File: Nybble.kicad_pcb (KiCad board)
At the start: 2 copper layers, 250.4 x 79 mm, 106 parts, among them J1 USB_mini_micro_B, SW1 SW_PUSH, U1 ATMEGA32U4, X1 XTAL_GND

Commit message: Starting to add traces to keyboard
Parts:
- moved C1 8.55 mm to (100.2, 86.0), turned to 45 degrees
- moved C2 4.56 mm to (96.2, 90.0), turned to 225 degrees
- moved C6 3.70 mm to (85.9, 90.7), turned to 270 degrees
- moved X1 2.16 mm to (95.6, 86.0), turned to 225 degrees
- moved R2 2.03 mm to (83.8, 90.9), turned to 270 degrees
- moved C7 1.91 mm to (84.0, 69.7)
- moved C3 1.30 mm to (77.6, 75.3), turned to 225 degrees
- turned SW1 to 180 degrees
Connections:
- MX27 pad 2: Net-(MX27-Pad2) -> Net-(D27-Pad2)
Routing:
- net VCC: track 0.00 -> 208.5 mm, vias 0 -> 4
- net Net-(C2-Pad1): track 0.00 -> 12.2 mm
- net Net-(R2-Pad1): track 0.00 -> 11.3 mm, vias 0 -> 2
- net Net-(C1-Pad1): track 0.00 -> 11.2 mm
- net Net-(R1-Pad2): track 0.00 -> 4.34 mm
- net Net-(C8-Pad1): track 0.00 -> 3.70 mm

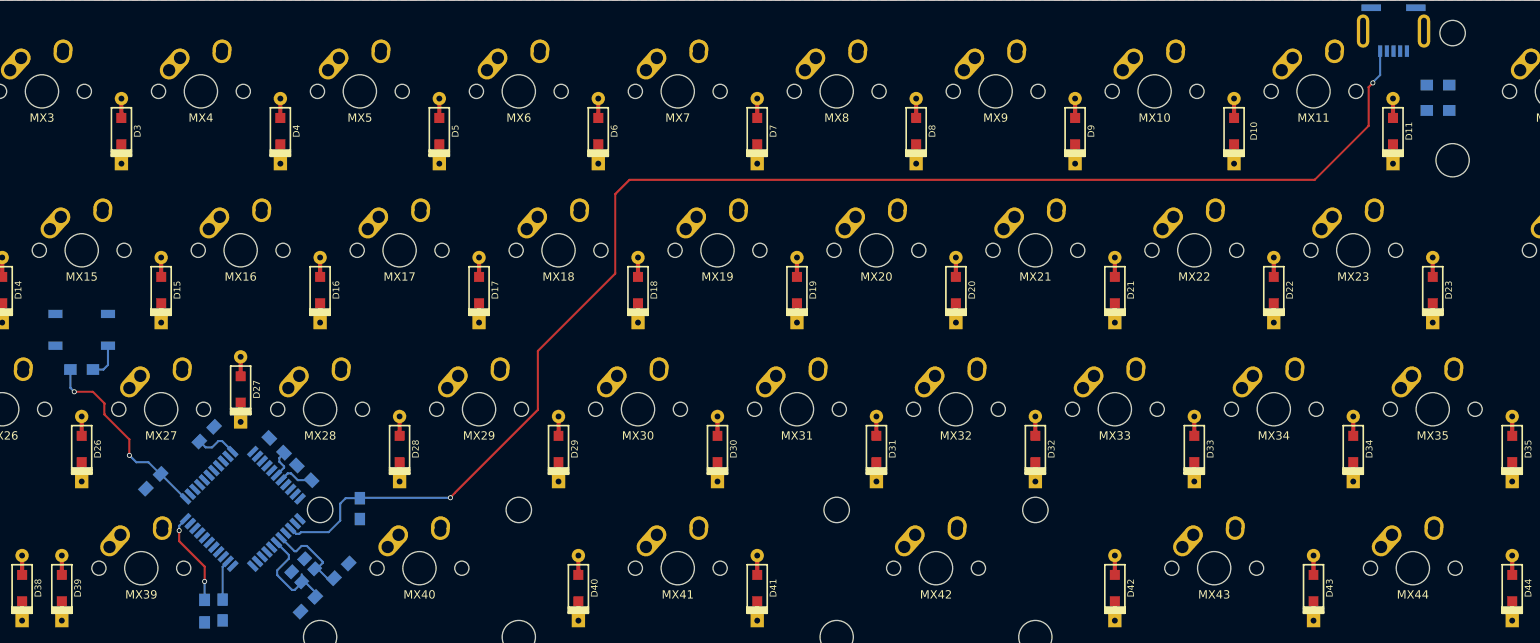
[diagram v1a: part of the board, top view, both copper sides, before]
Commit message: Fixed reset switch, and added a via between the two ground planes
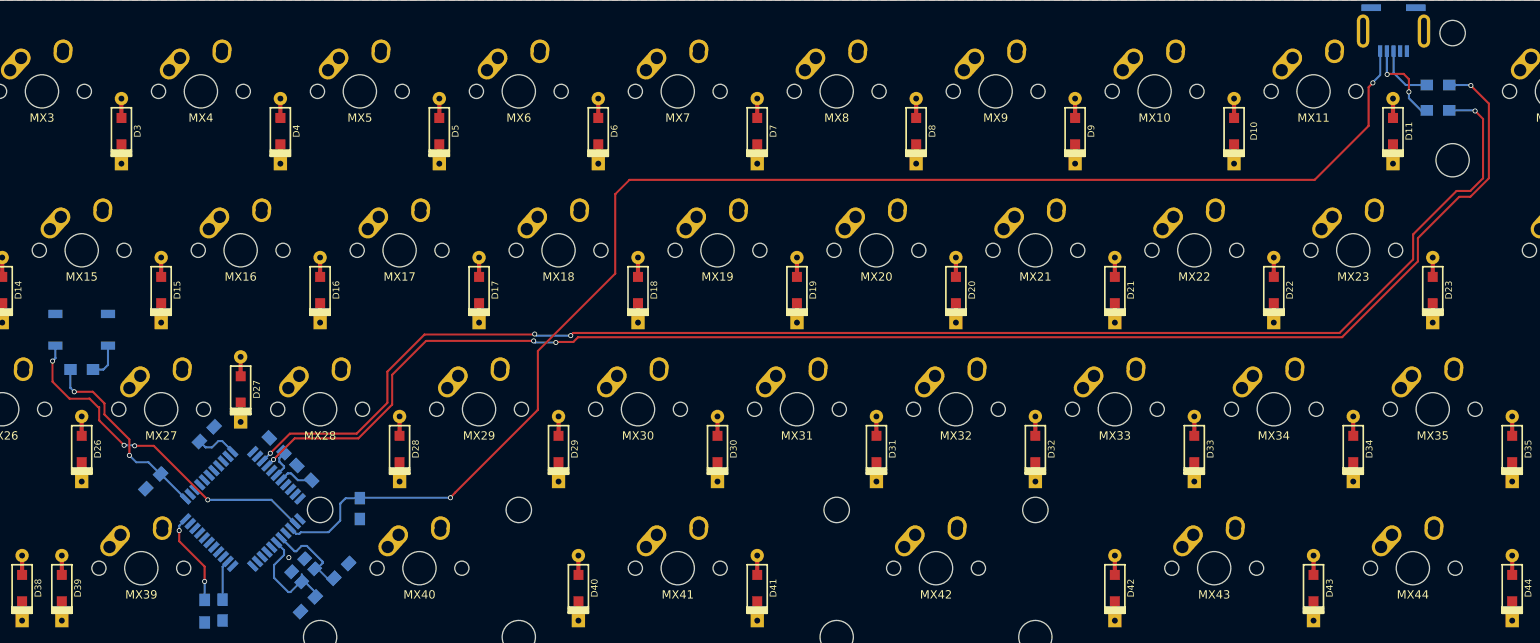
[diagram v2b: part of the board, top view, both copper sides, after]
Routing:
- net Net-(R4-Pad1): track 0.00 -> 179.2 mm, vias 0 -> 4
- net Net-(R3-Pad1): track 0.00 -> 176.0 mm, vias 0 -> 4
- net Net-(R1-Pad2): track 4.34 -> 45.9 mm, vias 0 -> 4
- net Net-(J1-Pad2): track 0.00 -> 10.7 mm, vias 0 -> 2
- net Net-(J1-Pad3): track 0.00 -> 7.19 mm
- net Net-(C2-Pad1): track 12.2 -> 12.7 mm
- net GND: track 0.00 -> 0.10 mm, vias 0 -> 1

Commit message: Finished the traces between the switches and the diodes
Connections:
- MX37 pad 1: Net-(MX37-Pad1) -> Net-(MX1-Pad1)
- MX38 pad 1: Net-(MX38-Pad1) -> Net-(MX14-Pad1)
- MX39 pad 2: Net-(MX39-Pad2) -> Net-(D39-Pad2)
- MX40 pad 2: Net-(MX40-Pad2) -> Net-(D40-Pad2)
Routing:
- net Net-(D42-Pad2): track 0.00 -> 20.2 mm
- net Net-(D40-Pad2): track 0.00 -> 18.8 mm
- net Net-(D39-Pad2): track 0.00 -> 17.6 mm
- net Net-(D12-Pad2): track 0.00 -> 16.4 mm
- net Net-(D24-Pad2): track 0.00 -> 15.1 mm
- net Net-(D25-Pad2): track 0.00 -> 13.8 mm
- net Net-(D11-Pad2): track 0.00 -> 13.7 mm
- net Net-(D13-Pad2): track 0.00 -> 13.2 mm
- net Net-(D37-Pad2): track 0.00 -> 11.9 mm
- net Net-(D10-Pad2): track 0.00 -> 11.7 mm
- net Net-(D3-Pad2): track 0.00 -> 11.7 mm
- net Net-(D43-Pad2): track 0.00 -> 11.6 mm
- net Net-(D30-Pad2): track 0.00 -> 11.5 mm
- net Net-(D29-Pad2): track 0.00 -> 11.4 mm
- net Net-(D22-Pad2): track 0.00 -> 11.4 mm
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
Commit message: Finished Wiring COlumns
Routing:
- net Net-(MX10-Pad1): track 0.00 -> 73.7 mm
- net Net-(MX21-Pad1): track 0.00 -> 68.0 mm
- net Net-(MX15-Pad1): track 0.00 -> 67.3 mm, vias 0 -> 1
- net Net-(MX14-Pad1): track 0.00 -> 66.5 mm
- net Net-(MX17-Pad1): track 0.00 -> 66.3 mm
- net Net-(MX1-Pad1): track 0.00 -> 65.6 mm
- net Net-(MX18-Pad1): track 0.00 -> 65.0 mm
- net Net-(MX20-Pad1): track 0.00 -> 64.4 mm
- net Net-(MX12-Pad1): track 0.00 -> 60.9 mm
- net Net-(MX19-Pad1): track 0.00 -> 44.9 mm
- net Net-(MX16-Pad1): track 0.00 -> 44.0 mm
- net Net-(MX11-Pad1): track 0.00 -> 44.0 mm, vias 0 -> 1

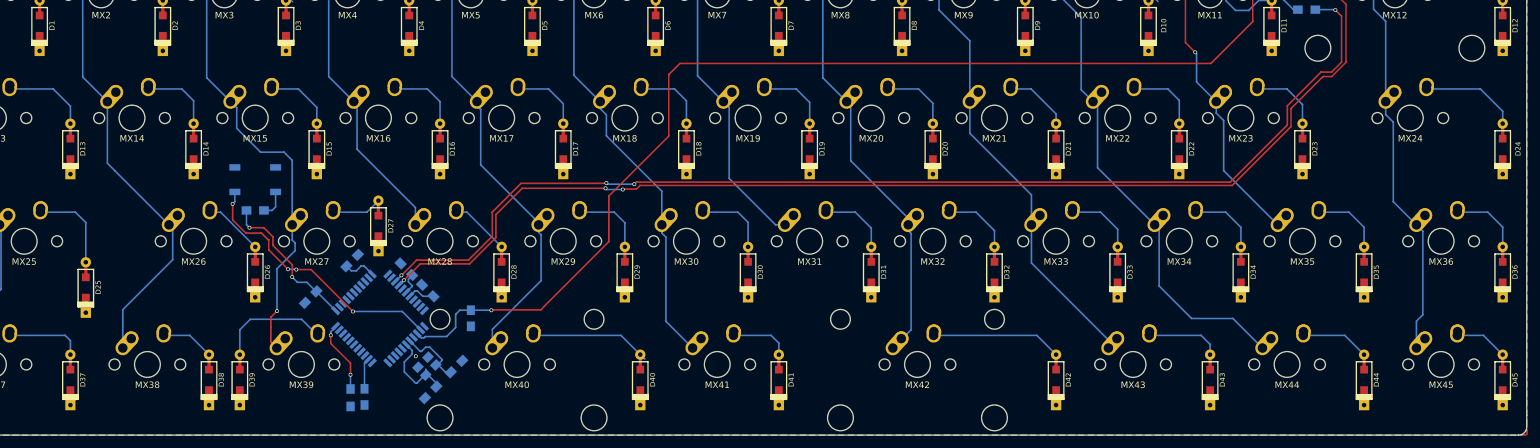
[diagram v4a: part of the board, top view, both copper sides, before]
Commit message: Finished routing the connections for the rows
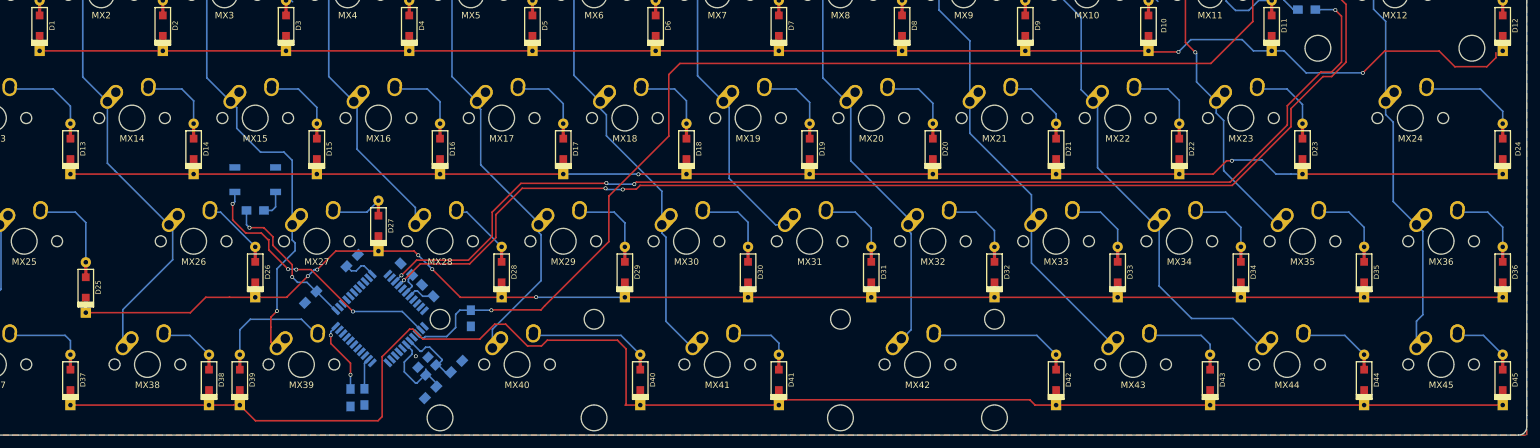
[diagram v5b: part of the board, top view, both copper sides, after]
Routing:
- net Net-(D37-Pad1): track 0.00 -> 248.1 mm
- net Net-(D1-Pad1): track 0.00 -> 231.9 mm, vias 0 -> 2
- net Net-(D25-Pad1): track 0.00 -> 226.1 mm, vias 0 -> 6
- net Net-(D13-Pad1): track 0.00 -> 223.3 mm, vias 0 -> 2
- net Net-(D40-Pad2): track 18.8 -> 17.8 mm

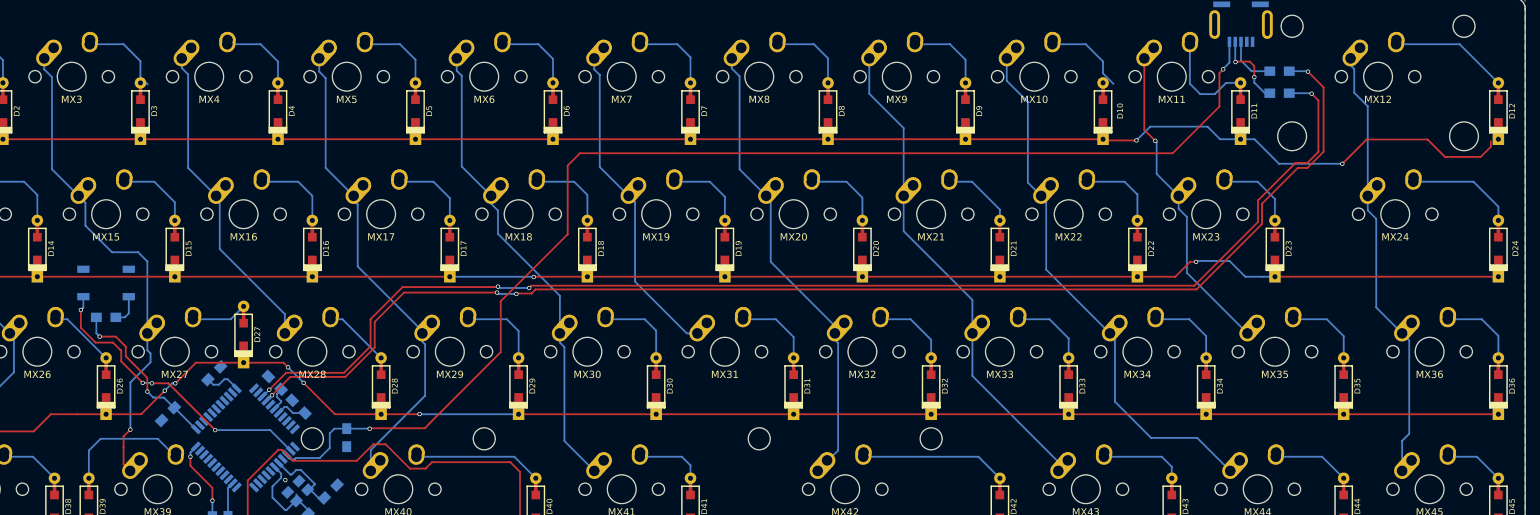
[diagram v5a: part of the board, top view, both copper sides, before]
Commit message: Fixed issues with row, and column traces
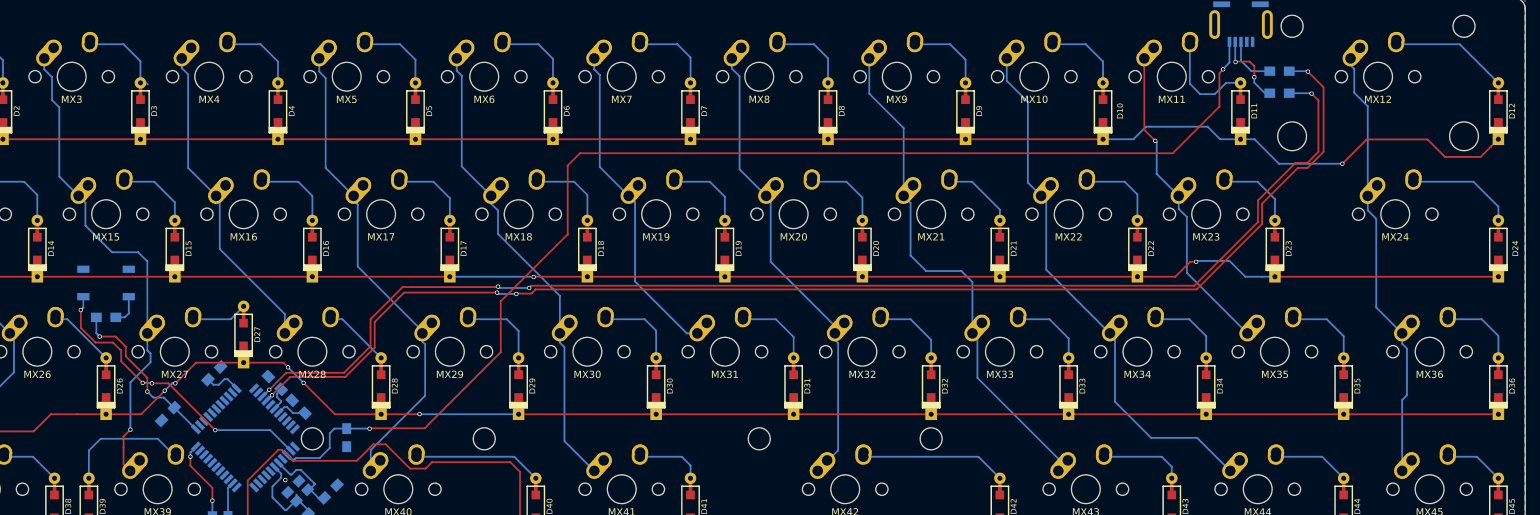
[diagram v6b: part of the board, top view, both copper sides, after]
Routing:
- net Net-(MX21-Pad1): track 68.0 -> 72.1 mm
- net Net-(D1-Pad1): track 231.9 -> 232.7 mm, vias 2 -> 1
- net Net-(D10-Pad2): track 11.7 -> 11.0 mm

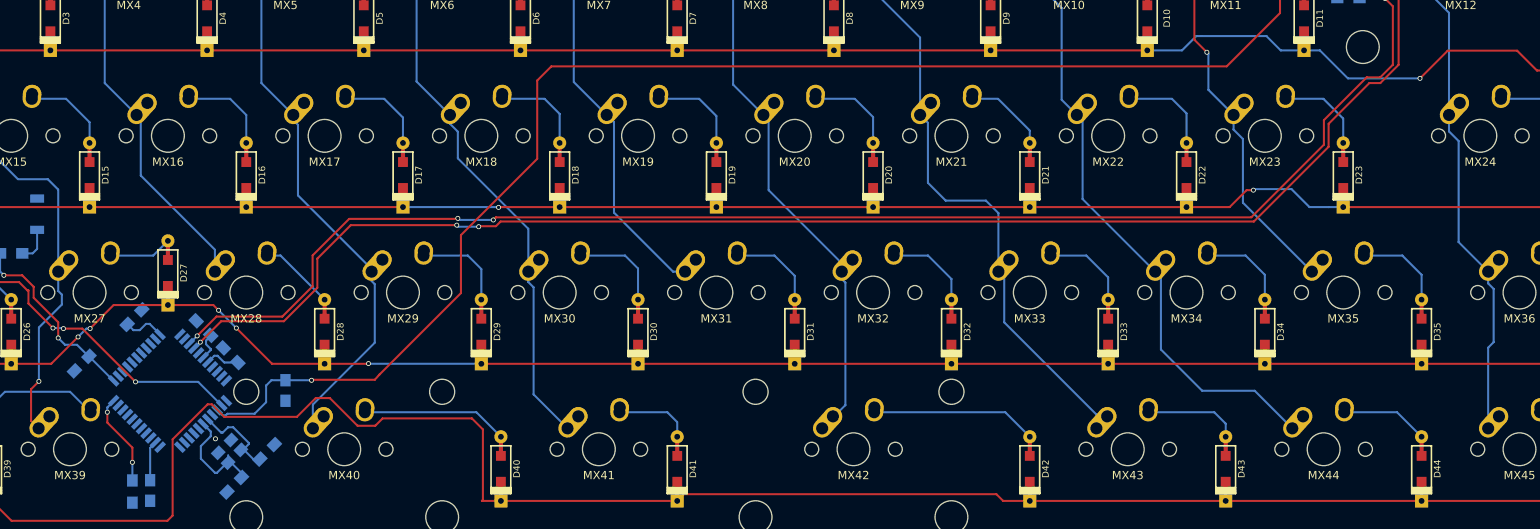
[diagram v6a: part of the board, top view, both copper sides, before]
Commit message: Wired up the rows for the pcb
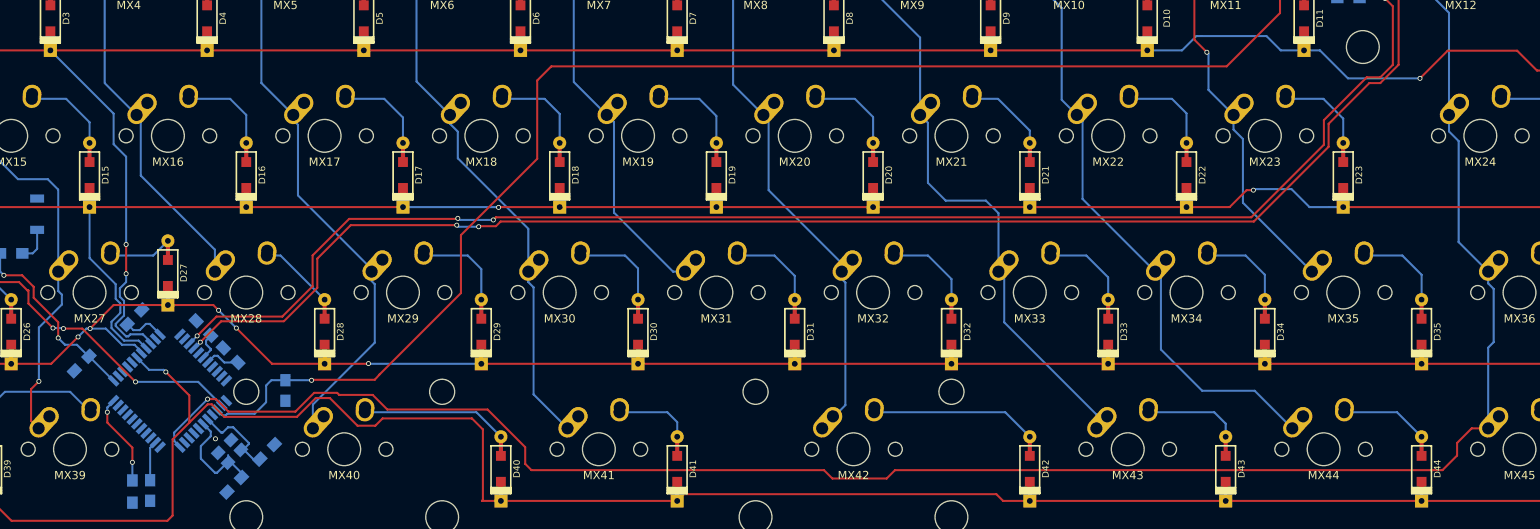
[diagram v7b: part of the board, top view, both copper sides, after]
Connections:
- D1 pad 1: Net-(D1-Pad1) -> /Row0
- D10 pad 1: Net-(D1-Pad1) -> /Row0
- D11 pad 1: Net-(D1-Pad1) -> /Row0
- D12 pad 1: Net-(D1-Pad1) -> /Row0
- D13 pad 1: Net-(D13-Pad1) -> /Row1
- D14 pad 1: Net-(D13-Pad1) -> /Row1
- D15 pad 1: Net-(D13-Pad1) -> /Row1
- D16 pad 1: Net-(D13-Pad1) -> /Row1
- D17 pad 1: Net-(D13-Pad1) -> /Row1
- D18 pad 1: Net-(D13-Pad1) -> /Row1
- D19 pad 1: Net-(D13-Pad1) -> /Row1
- D2 pad 1: Net-(D1-Pad1) -> /Row0
- D20 pad 1: Net-(D13-Pad1) -> /Row1
- D21 pad 1: Net-(D13-Pad1) -> /Row1
- D22 pad 1: Net-(D13-Pad1) -> /Row1
- D23 pad 1: Net-(D13-Pad1) -> /Row1
- D24 pad 1: Net-(D13-Pad1) -> /Row1
- D25 pad 1: Net-(D25-Pad1) -> /Row2
- D26 pad 1: Net-(D25-Pad1) -> /Row2
- D27 pad 1: Net-(D25-Pad1) -> /Row2
- D28 pad 1: Net-(D25-Pad1) -> /Row2
- D29 pad 1: Net-(D25-Pad1) -> /Row2
- D3 pad 1: Net-(D1-Pad1) -> /Row0
- D30 pad 1: Net-(D25-Pad1) -> /Row2
- D31 pad 1: Net-(D25-Pad1) -> /Row2
- D32 pad 1: Net-(D25-Pad1) -> /Row2
- D33 pad 1: Net-(D25-Pad1) -> /Row2
- D34 pad 1: Net-(D25-Pad1) -> /Row2
- D35 pad 1: Net-(D25-Pad1) -> /Row2
- D36 pad 1: Net-(D25-Pad1) -> /Row2
- D37 pad 1: Net-(D37-Pad1) -> /Row3
- D38 pad 1: Net-(D37-Pad1) -> /Row3
- D39 pad 1: Net-(D37-Pad1) -> /Row3
- D4 pad 1: Net-(D1-Pad1) -> /Row0
- D40 pad 1: Net-(D37-Pad1) -> /Row3
- D41 pad 1: Net-(D37-Pad1) -> /Row3
- D42 pad 1: Net-(D37-Pad1) -> /Row3
- D43 pad 1: Net-(D37-Pad1) -> /Row3
- D44 pad 1: Net-(D37-Pad1) -> /Row3
- D45 pad 1: Net-(D37-Pad1) -> /Row3
- D5 pad 1: Net-(D1-Pad1) -> /Row0
- D6 pad 1: Net-(D1-Pad1) -> /Row0
- D7 pad 1: Net-(D1-Pad1) -> /Row0
- D8 pad 1: Net-(D1-Pad1) -> /Row0
- D9 pad 1: Net-(D1-Pad1) -> /Row0
- MX1 pad 1: Net-(MX1-Pad1) -> /Col0
- MX10 pad 1: Net-(MX10-Pad1) -> /Col9
- MX11 pad 1: Net-(MX11-Pad1) -> /Col10
- MX12 pad 1: Net-(MX12-Pad1) -> /Col11
- MX13 pad 1: Net-(MX1-Pad1) -> /Col0
- MX14 pad 1: Net-(MX14-Pad1) -> /Col1
- MX15 pad 1: Net-(MX15-Pad1) -> /Col2
- MX16 pad 1: Net-(MX16-Pad1) -> /Col3
- MX17 pad 1: Net-(MX17-Pad1) -> /Col4
- MX18 pad 1: Net-(MX18-Pad1) -> /Col5
- MX19 pad 1: Net-(MX19-Pad1) -> /Col6
- MX2 pad 1: Net-(MX14-Pad1) -> /Col1
- MX20 pad 1: Net-(MX20-Pad1) -> /Col7
- MX21 pad 1: Net-(MX21-Pad1) -> /Col8
- MX22 pad 1: Net-(MX10-Pad1) -> /Col9
- MX23 pad 1: Net-(MX11-Pad1) -> /Col10
- MX24 pad 1: Net-(MX12-Pad1) -> /Col11
- MX25 pad 1: Net-(MX1-Pad1) -> /Col0
- MX26 pad 1: Net-(MX14-Pad1) -> /Col1
- MX27 pad 1: Net-(MX15-Pad1) -> /Col2
- MX28 pad 1: Net-(MX16-Pad1) -> /Col3
- MX29 pad 1: Net-(MX17-Pad1) -> /Col4
- MX3 pad 1: Net-(MX15-Pad1) -> /Col2
- MX30 pad 1: Net-(MX18-Pad1) -> /Col5
- MX31 pad 1: Net-(MX19-Pad1) -> /Col6
- MX32 pad 1: Net-(MX20-Pad1) -> /Col7
- MX33 pad 1: Net-(MX21-Pad1) -> /Col8
- MX34 pad 1: Net-(MX10-Pad1) -> /Col9
- MX35 pad 1: Net-(MX11-Pad1) -> /Col10
- MX36 pad 1: Net-(MX12-Pad1) -> /Col11
- MX37 pad 1: Net-(MX1-Pad1) -> /Col0
- MX38 pad 1: Net-(MX14-Pad1) -> /Col1
- MX39 pad 1: Net-(MX15-Pad1) -> /Col2
- MX4 pad 1: Net-(MX16-Pad1) -> /Col3
- MX40 pad 1: Net-(MX17-Pad1) -> /Col4
- MX41 pad 1: Net-(MX18-Pad1) -> /Col5
- MX42 pad 1: Net-(MX20-Pad1) -> /Col7
- MX43 pad 1: Net-(MX21-Pad1) -> /Col8
- MX44 pad 1: Net-(MX10-Pad1) -> /Col9
- MX45 pad 1: Net-(MX12-Pad1) -> /Col11
- MX5 pad 1: Net-(MX17-Pad1) -> /Col4
- MX6 pad 1: Net-(MX18-Pad1) -> /Col5
- MX7 pad 1: Net-(MX19-Pad1) -> /Col6
- MX8 pad 1: Net-(MX20-Pad1) -> /Col7
- MX9 pad 1: Net-(MX21-Pad1) -> /Col8
- U1 pad 22: /Col12 -> /Col11
- U1 pad 25: /Col11 -> /Col10
- U1 pad 26: /Col10 -> /Col9
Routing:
- net /Row0: track 0.00 -> 276.4 mm, vias 0 -> 3
- net /Row3: track 0.00 -> 259.7 mm, vias 0 -> 1
- net Net-(D37-Pad1): track 248.1 -> 0.00 mm
- net /Row1: track 0.00 -> 245.2 mm, vias 0 -> 2
- net /Col11: track 0.00 -> 234.6 mm, vias 0 -> 2
- net /Row2: track 0.00 -> 233.7 mm, vias 0 -> 6
- net Net-(D1-Pad1): track 232.7 -> 0.00 mm, vias 1 -> 0
- net Net-(D25-Pad1): track 226.1 -> 0.00 mm, vias 6 -> 0
- net Net-(D13-Pad1): track 223.3 -> 0.00 mm, vias 2 -> 0
- net Net-(MX10-Pad1): track 73.7 -> 0.00 mm
- net /Col9: track 0.00 -> 73.7 mm
- net Net-(MX21-Pad1): track 72.1 -> 0.00 mm
- net /Col8: track 0.00 -> 72.1 mm
- net Net-(MX15-Pad1): track 67.3 -> 0.00 mm, vias 1 -> 0
- net /Col2: track 0.00 -> 67.3 mm, vias 0 -> 1
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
